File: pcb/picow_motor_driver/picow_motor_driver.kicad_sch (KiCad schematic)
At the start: 21 parts, among them J1 Conn_01x02_Pin, J2 Conn_01x05_Pin, J3 Conn_01x04_Pin, U1 Pico

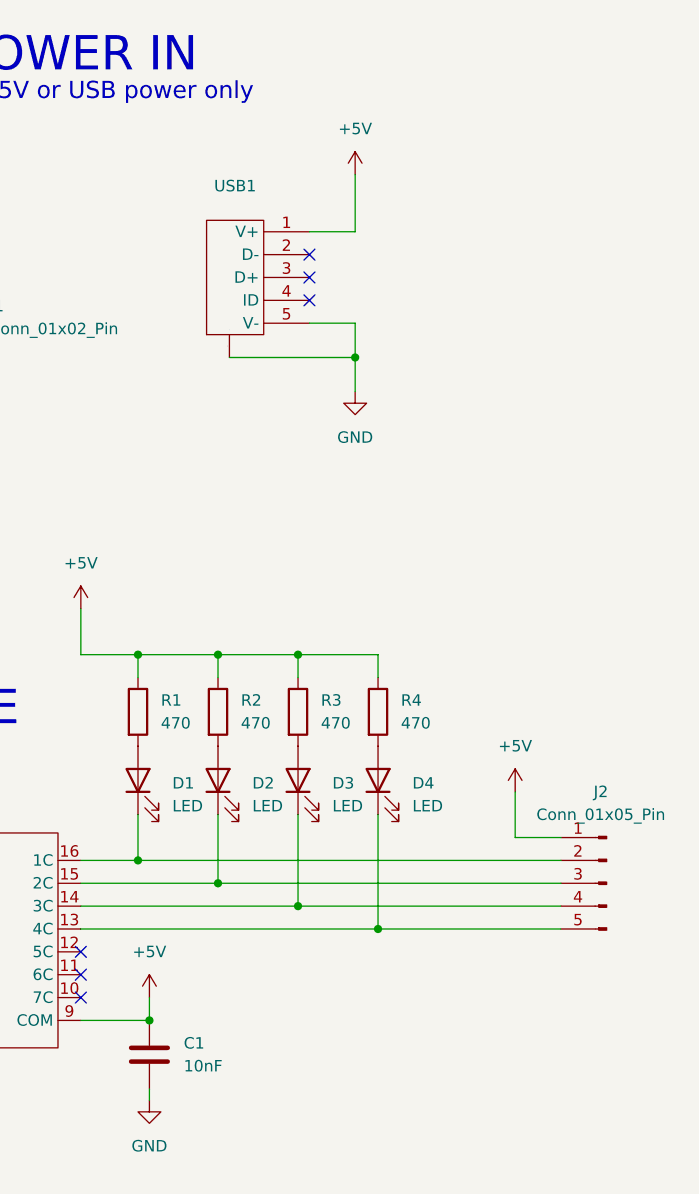
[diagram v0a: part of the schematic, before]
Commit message: Changed connectors out to JST, switched USB conn
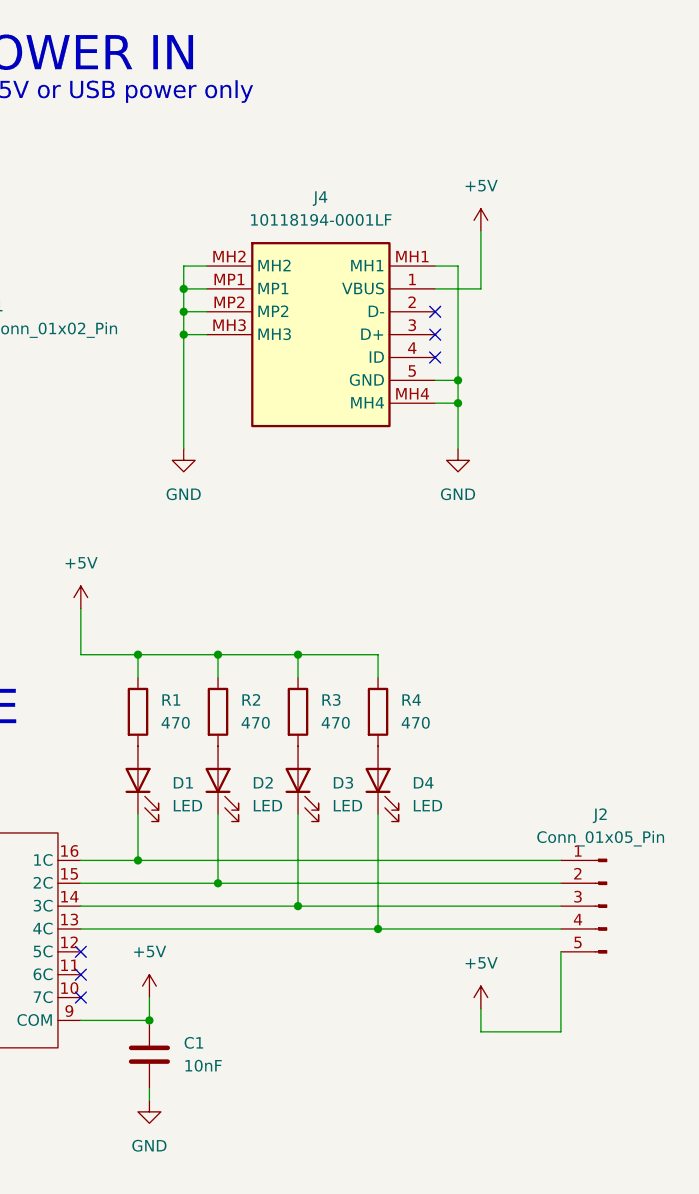
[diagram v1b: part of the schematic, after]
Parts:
- removed USB1: ~, Library:MICRO-USB-SMD_5P-P0.65-H-F_C10418, symbol New_Library:micro USBFemale
- added J4: 10118194-0001LF, Library:101181940001LF, symbol New_Library:10118194-0001LF
- J2: footprint Connector_PinHeader_2.54mm:PinHeader_1x05_P2.54mm_Horizontal -> Library:S5B-XH-A
- J3: footprint Connector_PinSocket_2.54mm:PinSocket_1x04_P2.54mm_Horizontal -> Library:S4BXHALFSN
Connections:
- net +5V: now also J2.5 (Pin_5), J4.1 (VBUS); no longer J2.1 (Pin_1)
- net GND: now also J4.5 (GND), J4.MH1, J4.MH2, J4.MH3, J4.MH4, J4.MP1, J4.MP2
- net at D4.1 (K), U2.13 (4C): now also J2.4 (Pin_4); no longer J2.5 (Pin_5)
- net at D1.1 (K), U2.16 (1C): now also J2.1 (Pin_1); no longer J2.2 (Pin_2)
- net at D2.1 (K), U2.15 (2C): now also J2.2 (Pin_2); no longer J2.3 (Pin_3)
- net at D3.1 (K), U2.14 (3C): now also J2.3 (Pin_3); no longer J2.4 (Pin_4)
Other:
- moved on the sheet: J2
